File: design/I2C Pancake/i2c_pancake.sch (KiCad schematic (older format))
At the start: 21 parts, among them J1 Conn_01x03, J2 Conn_01x03, J3 Conn_01x05_Male, J7 Conn_01x05_Male, J8 Conn_01x05_Female, SW1 SW_DIP_x04, U2 TL750M10CKVU, U6 PIC16F1826-ISO

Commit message: Revert "Add pinout labels to connectors"
This reverts commit 21ee90c71cbcb3ee9da454b06d43e90a118cf2fc.

Discard initial routing for the I2C Pancake board.

The routing will be done in a future commit with 4 copper layers.
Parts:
- C3: footprint footprints:C_0805_HandSoldering -> Capacitor_THT:C_Disc_D5.0mm_W2.5mm_P2.50mm
- F1: footprint Fuse:Fuse_1206_3216Metric_Pad1.42x1.75mm_HandSolder -> custom:littlefuse_01000020Z
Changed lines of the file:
@@
 F 0 "F1" V 1230 1200 50  0000 C CNN
 F 1 "Fuse" V 1075 1200 50  0000 C CNN
-F 2 "Fuse:Fuse_1206_3216Metric_Pad1.42x1.75mm_HandSolder" V 1080 1200 50  0001 C CNN
+F 2 "custom:littlefuse_01000020Z" V 1080 1200 50  0001 C CNN
 F 3 "" H 1150 1200 50  0001 C CNN
 	1    1150 1200
@@
 F 0 "C3" H 4615 1746 50  0000 L CNN
 F 1 "10 uF" H 4615 1655 50  0000 L CNN
-F 2 "footprints:C_0805_HandSoldering" H 4500 1700 50  0001 C CNN
+F 2 "Capacitor_THT:C_Disc_D5.0mm_W2.5mm_P2.50mm" H 4500 1700 50  0001 C CNN
 F 3 "~" H 4500 1700 50  0001 C CNN
 	1    4500 1700

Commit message: Create initial 4-layer routing for I2C Pancake Board.
This is my first attempt at doing 4-layer routing. There are
some outstanding issues with the routing here. Namely, the
coupling/decoupling capacitors have rather long traces
connecting them to their respective devices. These issues
will be fixed in future commits.
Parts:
- F1: symbol i2c_pancake-rescue:Fuse-device -> i2c_pancake-rescue:Fuse-device-i2c_pancake-rescue
- J1, J2: symbol i2c_pancake-rescue:Conn_01x03-strain_gauges_rtr-rescue -> i2c_pancake-rescue:Conn_01x03-strain_gauges_rtr-rescue-i2c_pancake-rescue
- R3, R5: symbol i2c_pancake-rescue:R-device -> i2c_pancake-rescue:R-device-i2c_pancake-rescue
- U6: symbol rlcsv3_modular-rescue:PIC16F1826-ISO -> i2c_pancake-rescue:PIC16F1826-ISO-rlcsv3_modular-rescue
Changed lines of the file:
@@
 $EndDescr
 $Comp
-L i2c_pancake-rescue:Conn_01x03-strain_gauges_rtr-rescue J1
+L i2c_pancake-rescue:Conn_01x03-strain_gauges_rtr-rescue-i2c_pancake-rescue J1
 U 1 1 5ACAED9B
 P 9100 1400
@@
 $EndComp
 $Comp
-L i2c_pancake-rescue:Conn_01x03-strain_gauges_rtr-rescue J2
+L i2c_pancake-rescue:Conn_01x03-strain_gauges_rtr-rescue-i2c_pancake-rescue J2
 U 1 1 5ACAEDA8
 P 9100 2250
@@
 $EndComp
 $Comp
-L i2c_pancake-rescue:R-device R3
+L i2c_pancake-rescue:R-device-i2c_pancake-rescue R3
 U 1 1 5ACAEDCA
 P 4500 4000
@@
 $EndComp
 $Comp
-L i2c_pancake-rescue:R-device R5
+L i2c_pancake-rescue:R-device-i2c_pancake-rescue R5
 U 1 1 5ACAEDD1
 P 4500 4350
@@
 	3500 5850 3250 5850
 $Comp
-L i2c_pancake-rescue:Fuse-device F1
+L i2c_pancake-rescue:Fuse-device-i2c_pancake-rescue F1
 U 1 1 5ACB8796
 P 1150 1200
@@
 Connection ~ 4500 4200
 $Comp
-L rlcsv3_modular-rescue:PIC16F1826-ISO U6
+L i2c_pancake-rescue:PIC16F1826-ISO-rlcsv3_modular-rescue U6
 U 1 1 5E74C816
 P 5850 3550

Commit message: Increase I2C line clearance to 20 mils.
This will minimize cross-talk with I2C lines.
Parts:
- C1, C3: symbol Device:CP1 -> Device:C
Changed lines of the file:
@@
 $EndComp
 $Comp
-L Device:CP1 C1
+L Device:C C1
 U 1 1 5EAAE718
 P 1500 1700
@@
 $EndComp
 $Comp
-L Device:CP1 C3
+L Device:C C3
 U 1 1 5EAAF20A
 P 4500 1700

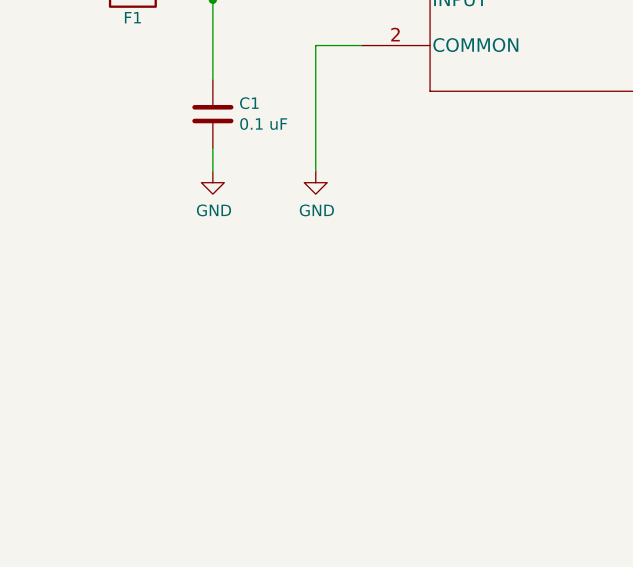
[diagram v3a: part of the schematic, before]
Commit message: Replace fuse footprint with standard 0805 SMD footprint.
A note has been added to the schematic regarding expected current
and trip current through the fuse.
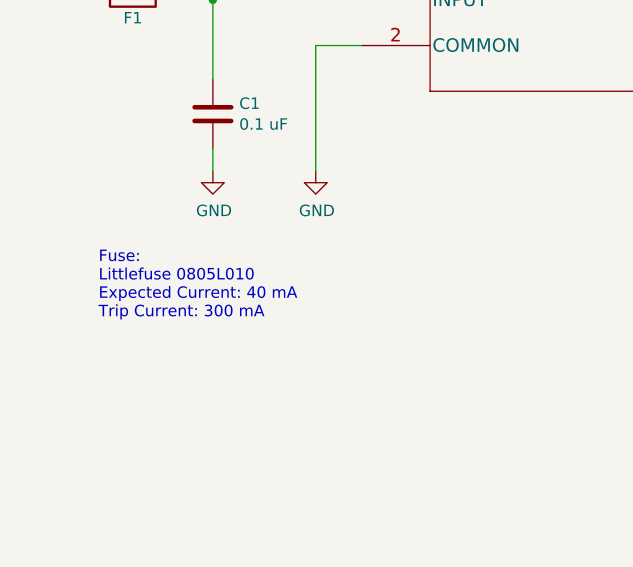
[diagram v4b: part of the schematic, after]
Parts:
- C3: footprint Capacitor_THT:C_Disc_D5.0mm_W2.5mm_P2.50mm -> Capacitor_SMD:C_0805_2012Metric_Pad1.15x1.40mm_HandSolder
- F1: footprint custom:littlefuse_01000020Z -> Fuse:Fuse_0805_2012Metric_Pad1.15x1.40mm_HandSolder
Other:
- note added: "Fuse:\nLittlefuse 0805L010\nExpected Current: 40 mA\nTrip Current: 300 mA"
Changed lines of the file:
@@
 F 0 "F1" V 1230 1200 50  0000 C CNN
 F 1 "Fuse" V 1075 1200 50  0000 C CNN
-F 2 "custom:littlefuse_01000020Z" V 1080 1200 50  0001 C CNN
+F 2 "Fuse:Fuse_0805_2012Metric_Pad1.15x1.40mm_HandSolder" V 1080 1200 50  0001 C CNN
 F 3 "" H 1150 1200 50  0001 C CNN
 	1    1150 1200
@@
 F 0 "C3" H 4615 1746 50  0000 L CNN
 F 1 "10 uF" H 4615 1655 50  0000 L CNN
-F 2 "Capacitor_THT:C_Disc_D5.0mm_W2.5mm_P2.50mm" H 4500 1700 50  0001 C CNN
+F 2 "Capacitor_SMD:C_0805_2012Metric_Pad1.15x1.40mm_HandSolder" H 4500 1700 50  0001 C CNN
 F 3 "~" H 4500 1700 50  0001 C CNN
 	1    4500 1700
@@
 	4850 1200 4850 1000
 Connection ~ 4500 1200
+Text Notes 1000 2600 0    50   ~ 0
+Fuse:\nLittlefuse 0805L010\nExpected Current: 40 mA\nTrip Current: 300 mA
 $EndSCHEMATC

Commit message: Add test points to the Pancake board.
Test points were added to the outputs of each strain guage amp.
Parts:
- C3: footprint Capacitor_SMD:C_0805_2012Metric_Pad1.15x1.40mm_HandSolder -> footprints:C_0805_HandSoldering
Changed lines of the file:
@@
-	1    0    0    -1
-$EndComp
-$Comp
-L Device:C C3
-U 1 1 5EAAF20A
-P 4500 1700
-F 0 "C3" H 4615 1746 50  0000 L CNN
-F 1 "10 uF" H 4615 1655 50  0000 L CNN
-F 2 "Capacitor_SMD:C_0805_2012Metric_Pad1.15x1.40mm_HandSolder" H 4500 1700 50  0001 C CNN
-F 3 "~" H 4500 1700 50  0001 C CNN
-	1    4500 1700
 	1    0    0    -1
 $EndComp
@@
 Text Notes 1000 2600 0    50   ~ 0
 Fuse:\nLittlefuse 0805L010\nExpected Current: 40 mA\nTrip Current: 300 mA
+$Comp
+L Device:C C3
+U 1 1 5EAAF20A
+P 4500 1700
+F 0 "C3" H 4615 1746 50  0000 L CNN
+F 1 "10 uF" H 4615 1655 50  0000 L CNN
+F 2 "footprints:C_0805_HandSoldering" H 4500 1700 50  0001 C CNN
+F 3 "~" H 4500 1700 50  0001 C CNN
+	1    4500 1700
+	1    0    0    -1
+$EndComp
 $EndSCHEMATC

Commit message: Implement improvements suggested by Zachariah Mears and update Gerbers
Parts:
- R2: renamed from R3; value 5K -> 10K
- R3: renamed from R5; value 10K -> 5K
- renumbered C3 to C2, C8 to C3, J3 to J1, J7 to J2, J1 to J3, J2 to J4, J8 to J5, R15 to R1, R17 to R4, R12 to R5, R13 to R6, R14 to R7, R16 to R8, U2 to U1, U6 to U2

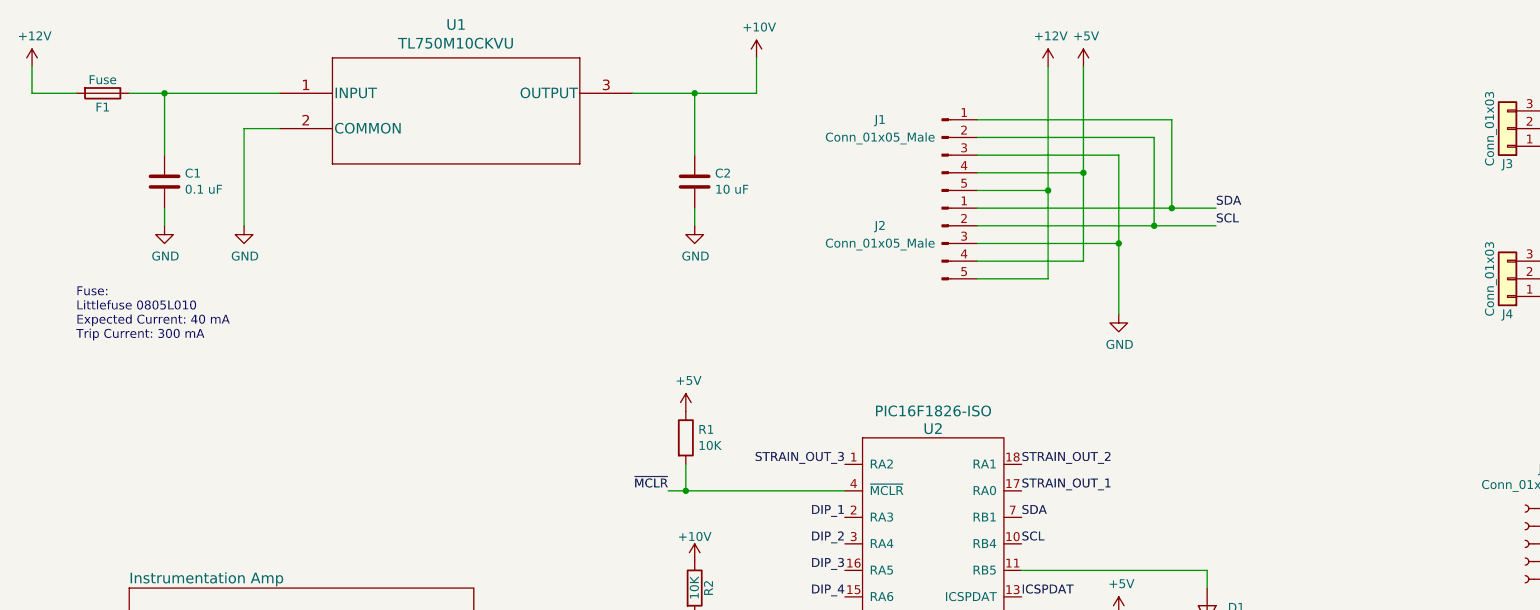
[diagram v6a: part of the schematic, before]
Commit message: Replace linear regulator to match the recent Digikey order
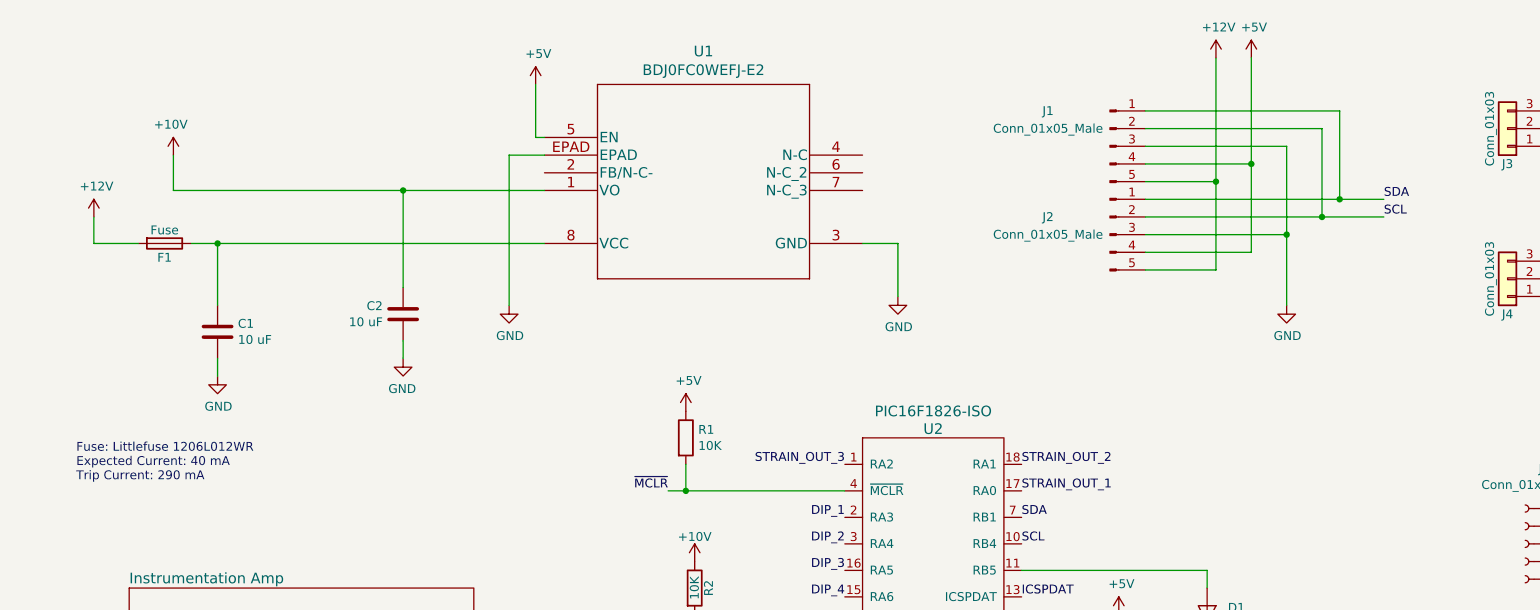
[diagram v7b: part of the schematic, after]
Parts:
- removed U1: TL750M10CKVU, footprints:TL750M10CKVU, symbol tlv750m10:TL750M05CKVURG3
- added U1: BDJ0FC0WEFJ-E2, footprints:BDJ0FC0WEFJ-E2, symbol BDJ0FC0WEFJ-E2:BDJ0FC0WEFJ-E2
- C1: value 0.1 uF -> 10 uF
- F1: footprint Fuse:Fuse_0805_2012Metric_Pad1.15x1.40mm_HandSolder -> Fuse:Fuse_1206_3216Metric_Pad1.42x1.75mm_HandSolder
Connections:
- net +10V: now also U1.1 (VO)
- net +5V: now also U1.5 (EN)
- net GND: now also U1.3 (GND), U1.EPAD
- net at C1.1, F1.1: now also U1.8 (VCC)
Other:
- note added: "Fuse: Littlefuse 1206L012WR\nExpected Current: 40 mA\nTrip Current: 290 mA"
- note removed: "Fuse:\nLittlefuse 0805L010\nExpected Current: 40 mA\nTrip Current: 300 mA"
- moved on the sheet: C1, C2, F1, J1, J2

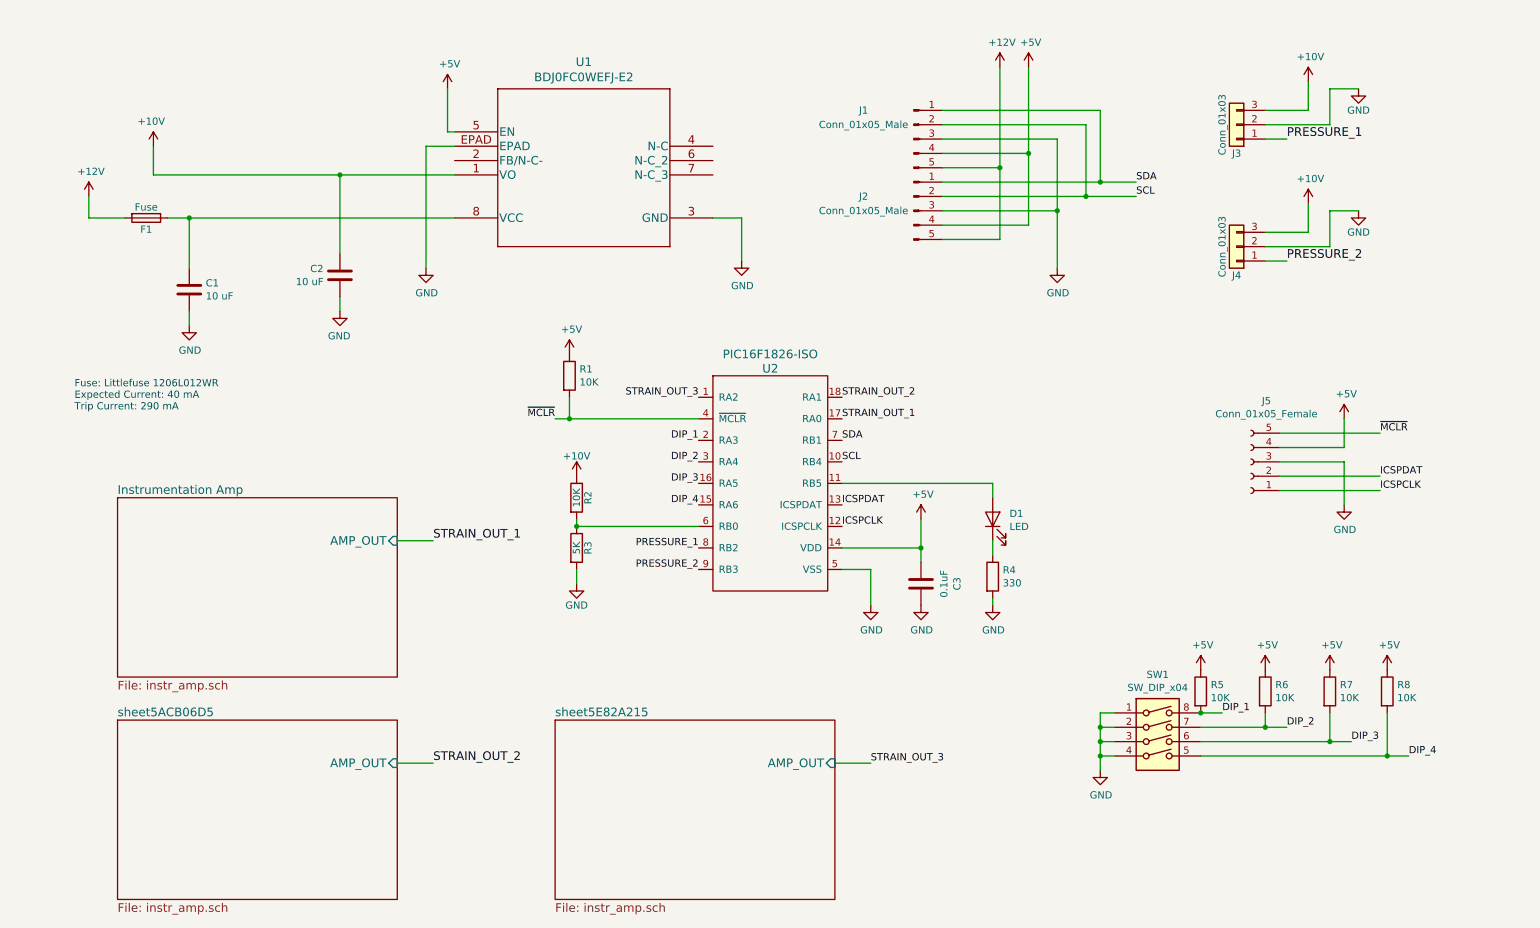
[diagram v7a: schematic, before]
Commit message: Add RC filters to the analog inputs of the PIC
This commit also includes a new and improved routing.
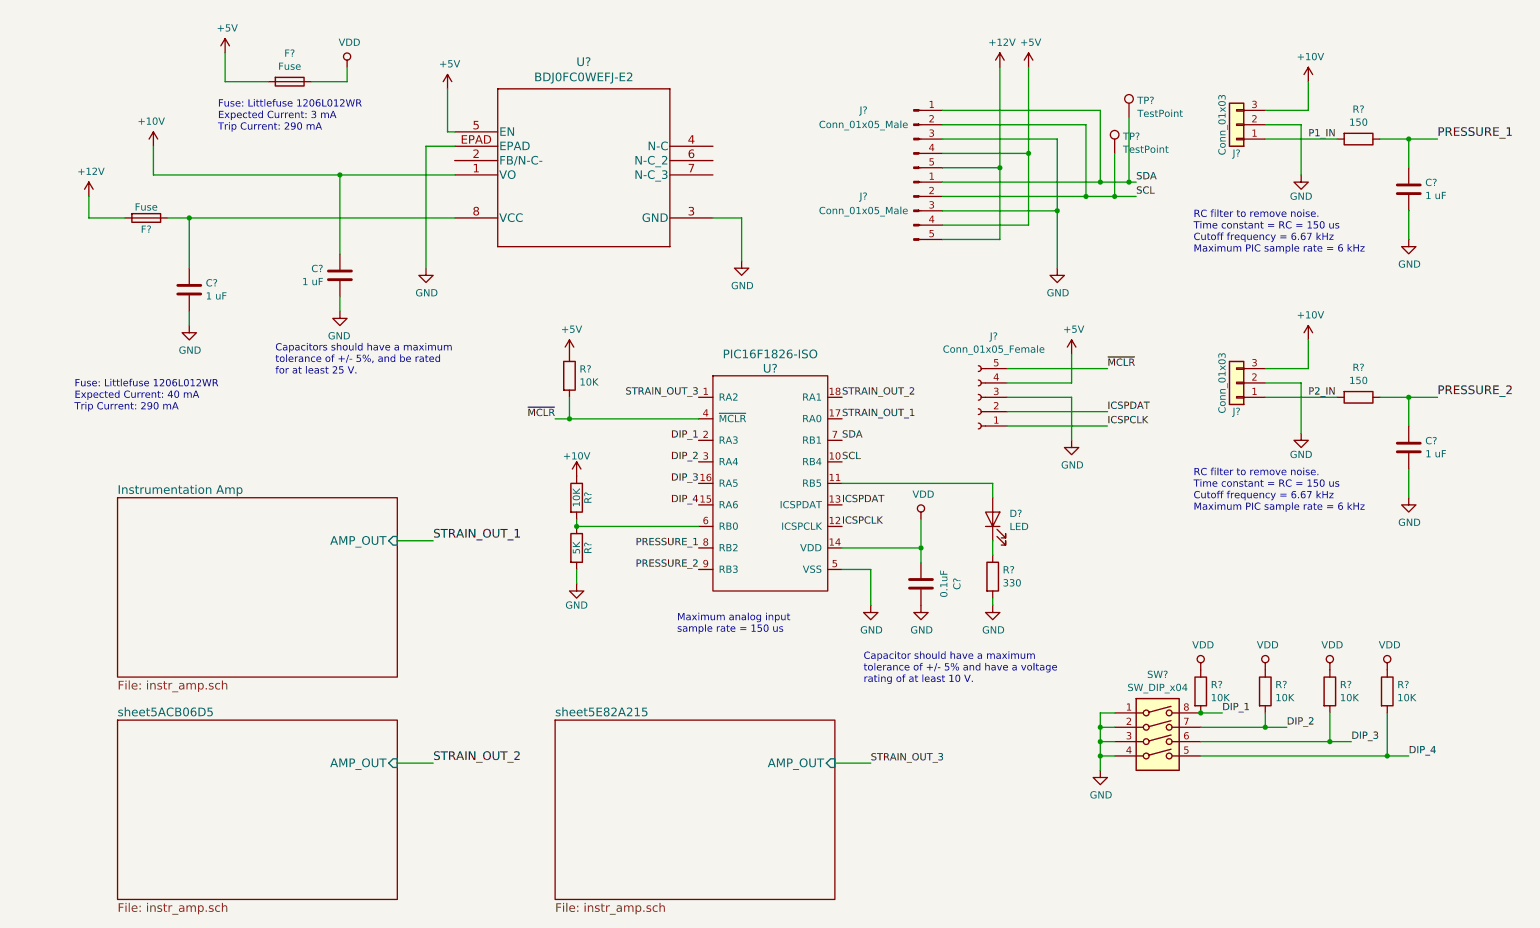
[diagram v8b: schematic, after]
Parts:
- removed J4: Conn_01x03, TerminalBlock_Phoenix:TerminalBlock_Phoenix_MKDS-1,5-3_1x03_P5.00mm_Horizontal, symbol i2c_pancake-rescue:Conn_01x03-strain_gauges_rtr-rescue-i2c_pancake-rescue
- added C? (x2): 1 uF, footprints:C_0805_HandSoldering, symbol Device:C
- added F?: Fuse, Fuse:Fuse_1206_3216Metric, symbol Device:Fuse
- added J?: Conn_01x03, TerminalBlock_Phoenix:TerminalBlock_Phoenix_MKDS-1,5-3_1x03_P5.00mm_Horizontal, symbol i2c_pancake-rescue:Conn_01x03-strain_gauges_rtr-rescue-i2c_pancake-rescue
- added R? (x2): 150, footprints:R_0805_HandSoldering, symbol Device:R
- added TP? (x2): TestPoint, custom:TestPoint, symbol Connector:TestPoint
- C?: renamed from C1; value 10 uF -> 1 uF
- C?: renamed from C2; value 10 uF -> 1 uF
- renumbered C3 to C?, D1 to D?, F1 to F?, J3 to J?, J5 to J?, J1 to J?, J2 to J?, R2 to R?, R3 to R?, R5 to R?, R6 to R?, R7 to R?, R8 to R?, R1 to R?, R4 to R?, SW1 to SW?, U2 to U?, U1 to U?
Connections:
- net +10V: now also J?.3 (Pin_3)
- net +5V: now also F?.2; no longer C?.2, R?.1, R?.1, R?.1, R?.1, U?.14 (VDD)
- net GND: now also C?.2, C?.2, J?.2 (Pin_2)
- net PRESSURE_1: now also C?.1, R?.1; no longer J?.1 (Pin_1)
- net PRESSURE_2: now also C?.1, R?.1
- net SCL: now also TP?.1
- net SDA: now also TP?.1
- new net P1_IN: J?.1 (Pin_1), R?.2
- new net P2_IN: J?.1 (Pin_1), R?.2
- new net VDD: C?.2, F?.1, R?.1, R?.1, R?.1, R?.1, U?.14 (VDD)
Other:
- note added: "Capacitor should have a maximum\ntolerance of +/- 5% and have a voltage\nrating of at least 10 V."
- note added: "Capacitors should have a maximum\ntolerance of +/- 5%, and be rated \nfor at least 25 V."
- note added: "Fuse: Littlefuse 1206L012WR\nExpected Current: 3 mA\nTrip Current: 290 mA"
- note added: "Maximum analog input\nsample rate = 150 us"
- note added: "RC filter to remove noise. \nTime constant = RC = 150 us\nCutoff frequency = 6.67 kHz\nMaximum PIC sample rate = 6 kHz"
- moved on the sheet: J?
